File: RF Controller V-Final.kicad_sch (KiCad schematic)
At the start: 36 parts, among them J2 J_OLED, J3 BAT+, J4 BAT-, SW1 EG1218, U1 Teensy4.0, U3 NRF24L01, U5 AP2112K-3.3, U7 Pitch/Roll, U8 TPS542025DDCR, U9 Throttle/Yaw

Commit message: Modified regulator resistors
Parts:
- R6: value 13.3k -> 51.1k
- R7: value 100k -> 22k
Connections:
- net 9V_IN: now also R6.2; no longer R7.2
- net GND: now also R7.1; no longer R6.1
- new net: R6.1, R7.2, U8.5 (EN)
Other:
- moved on the sheet: R6, R7
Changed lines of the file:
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@@
 	)
 	(junction
-		(at 27.94 64.77)
+		(at 250.19 35.56)
 		(diameter 0)
 		(color 0 0 0 0)
 	)
 	(junction
-		(at 250.19 35.56)
+		(at 27.94 64.77)
 		(diameter 0)
 		(color 0 0 0 0)
@@
 	(wire
 		(pts
-			(xy 30.48 67.31) (xy 30.48 64.77)
-		)
-		(stroke
-			(width 0)
-			(type default)
-		)
-	)
-	(wire
-		(pts
 			(xy 213.36 82.55) (xy 212.09 82.55)
 		)
@@
 	(wire
 		(pts
-			(xy 27.94 72.39) (xy 30.48 72.39)
+			(xy 30.48 67.31) (xy 30.48 64.77)
 		)
 		(stroke
@@
 		)
 	)
-	(wire
-		(pts
-			(xy 27.94 63.5) (xy 27.94 64.77)
-		)
-		(stroke
-			(width 0)
-			(type default)
-		)
-	)
 	(polyline
 		(pts
@@
 		)
 	)
+	(wire
+		(pts
+			(xy 27.94 64.77) (xy 30.48 64.77)
+		)
+		(stroke
+			(width 0)
+			(type default)
+		)
+	)
 	(polyline
 		(pts
@@
 		)
 	)
+	(wire
+		(pts
+			(xy 27.94 63.5) (xy 27.94 64.77)
+		)
+		(stroke
+			(width 0)
+			(type default)
+		)
+	)
 	(polyline
 		(pts
@@
 		)
 	)
-	(wire
-		(pts
-			(xy 27.94 64.77) (xy 30.48 64.77)
-		)
-		(stroke
-			(width 0)
-			(type default)
-		)
-	)
 	(polyline
 		(pts
@@
 		)
 	)
+	(wire
+		(pts
+			(xy 27.94 72.39) (xy 30.48 72.39)
+		)
+		(stroke
+			(width 0)
+			(type default)
+		)
+	)
 	(polyline
 		(pts
@@
 	(symbol
 		(lib_id "Device:R")
-		(at 27.94 76.2 180)
+		(at 27.94 68.58 180)
 		(unit 1)
 		(body_style 1)
@@
 		(dnp no)
 		(property "Reference" "R6"
-			(at 24.638 77.47 0)
+			(at 24.638 69.85 0)
 			(show_name no)
 			(do_not_autoplace no)
@@
 			)
 		)
-		(property "Value" "13.3k"
-			(at 23.876 75.184 0)
+		(property "Value" "51.1k"
+			(at 23.876 67.564 0)
 			(show_name no)
 			(do_not_autoplace no)
@@
 		)
 		(property "Footprint" "Resistor_SMD:R_0805_2012Metric_Pad1.20x1.40mm_HandSolder"
-			(at 27.94 76.2 0)
+			(at 27.94 68.58 0)
 			(hide yes)
 			(show_name no)
@@
 		)
 		(property "Datasheet" ""
-			(at 27.94 76.2 0)
+			(at 27.94 68.58 0)
 			(hide yes)
 			(show_name no)
@@
 		)
 		(property "Description" "TPS542025 EN divider, VIN upper resistor"
-			(at 27.94 76.2 0)
+			(at 27.94 68.58 0)
 			(hide yes)
 			(show_name no)
@@
 	(symbol
 		(lib_id "Device:R")
-		(at 27.94 68.58 180)
+		(at 27.94 76.2 180)
 		(unit 1)
 		(body_style 1)
@@
 		(dnp no)
 		(property "Reference" "R7"
-			(at 26.416 69.85 0)
+			(at 26.416 77.47 0)
 			(show_name no)
 			(do_not_autoplace no)
@@
 			)
 		)
-		(property "Value" "100k"
-			(at 26.416 67.31 0)
+		(property "Value" "22k"
+			(at 26.416 74.93 0)
 			(show_name no)
 			(do_not_autoplace no)
@@
 		)
 		(property "Footprint" "Resistor_SMD:R_0805_2012Metric_Pad1.20x1.40mm_HandSolder"
-			(at 27.94 68.58 0)
+			(at 27.94 76.2 0)
 			(hide yes)
 			(show_name no)
@@
 		)
 		(property "Datasheet" ""
-			(at 27.94 68.58 0)
+			(at 27.94 76.2 0)
 			(hide yes)
 			(show_name no)
@@
 		)
 		(property "Description" "TPS542025 EN divider, ground lower resistor"
-			(at 27.94 68.58 0)
+			(at 27.94 76.2 0)
 			(hide yes)
 			(show_name no)
@@
 	)
 	(symbol
+		(lib_id "power:GND")
+		(at 27.94 80.01 0)
+		(unit 1)
+		(body_style 1)
+		(exclude_from_sim no)
+		(in_bom yes)
+		(on_board yes)
+		(in_pos_files yes)
+		(dnp no)
+		(fields_autoplaced yes)
+		(property "Reference" "#PWR05"
+			(at 27.94 86.36 0)
+			(hide yes)
+			(show_name no)
+			(do_not_autoplace no)
+			(effects
+				(font
+					(size 1.27 1.27)
+				)
+			)
+		)
+		(property "Value" "GND"
+			(at 27.94 85.09 0)
+			(show_name no)
+			(do_not_autoplace no)
+			(effects
+				(font
+					(size 1.27 1.27)
+				)
+			)
+		)
+		(property "Footprint" ""
+			(at 27.94 80.01 0)
+			(hide yes)
+			(show_name no)
+			(do_not_autoplace no)
+			(effects
+				(font
+					(size 1.27 1.27)
+				)
+			)
+		)
+		(property "Datasheet" ""
+			(at 27.94 80.01 0)
+			(hide yes)
+			(show_name no)
+			(do_not_autoplace no)
+			(effects
+				(font
+					(size 1.27 1.27)
+				)
+			)
+		)
+		(property "Description" "Power symbol creates a global label with name \"GND\" , ground"
+			(at 27.94 80.01 0)
+			(hide yes)
+			(show_name no)
+			(do_not_autoplace no)
+			(effects
+				(font
+					(size 1.27 1.27)
+				)
+			)
+		)
+		(pin "1"
+		)
+		(instances
+			(project "RF Controller V-Final"
+				(path "/20b51a64-697d-4081-9410-2d5c496e59fa"
+					(reference "#PWR05")
+					(unit 1)
+				)
+			)
+		)
+	)
+	(symbol
 		(lib_id "V2Components:TPS542025")
 		(at 40.64 69.85 0)
@@
 					(unit 1)
 				)
-			)
-		)
-	)
-	(symbol
-		(lib_id "power:GND")
-		(at 27.94 80.01 0)
-		(unit 1)
-		(body_style 1)
-		(exclude_from_sim no)
-		(in_bom yes)
-		(on_board yes)
-		(in_pos_files yes)
-		(dnp no)
-		(fields_autoplaced yes)
-		(property "Reference" "#PWR05"
-			(at 27.94 86.36 0)
-			(hide yes)
-			(show_name no)
-			(do_not_autoplace no)
-			(effects
-				(font
-					(size 1.27 1.27)
-				)
-			)
-		)
-		(property "Value" "GND"
-			(at 27.94 85.09 0)
-			(show_name no)
-			(do_not_autoplace no)
-			(effects
-				(font
-					(size 1.27 1.27)
-				)
-			)
-		)
-		(property "Footprint" ""
-			(at 27.94 80.01 0)
-			(hide yes)
-			(show_name no)
-			(do_not_autoplace no)
-			(effects
-				(font
-					(size 1.27 1.27)
-				)
-			)
-		)
-		(property "Datasheet" ""
-			(at 27.94 80.01 0)
-			(hide yes)
-			(show_name no)
-			(do_not_autoplace no)
-			(effects
-				(font
-					(size 1.27 1.27)
-				)
-			)
-		)
-		(property "Description" "Power symbol creates a global label with name \"GND\" , ground"
-			(at 27.94 80.01 0)
-			(hide yes)
-			(show_name no)
-			(do_not_autoplace no)
-			(effects
-				(font
-					(size 1.27 1.27)
-				)
-			)
-		)
-		(pin "1"
-		)
-		(instances
-			(project "RF Controller V-Final"
-				(path "/20b51a64-697d-4081-9410-2d5c496e59fa"
-					(reference "#PWR05")
-					(unit 1)
-				)

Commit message: Modified resistor for 5.5V EN startup
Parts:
- R6: value 51.1k -> 71.5k
- R7: value 22k -> 20k
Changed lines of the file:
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@@
 			)
 		)
-		(property "Value" "51.1k"
+		(property "Value" "71.5k"
 			(at 23.876 67.564 0)
 			(show_name no)
@@
 			)
 		)
-		(property "Value" "22k"
+		(property "Value" "20k"
 			(at 26.416 74.93 0)
 			(show_name no)

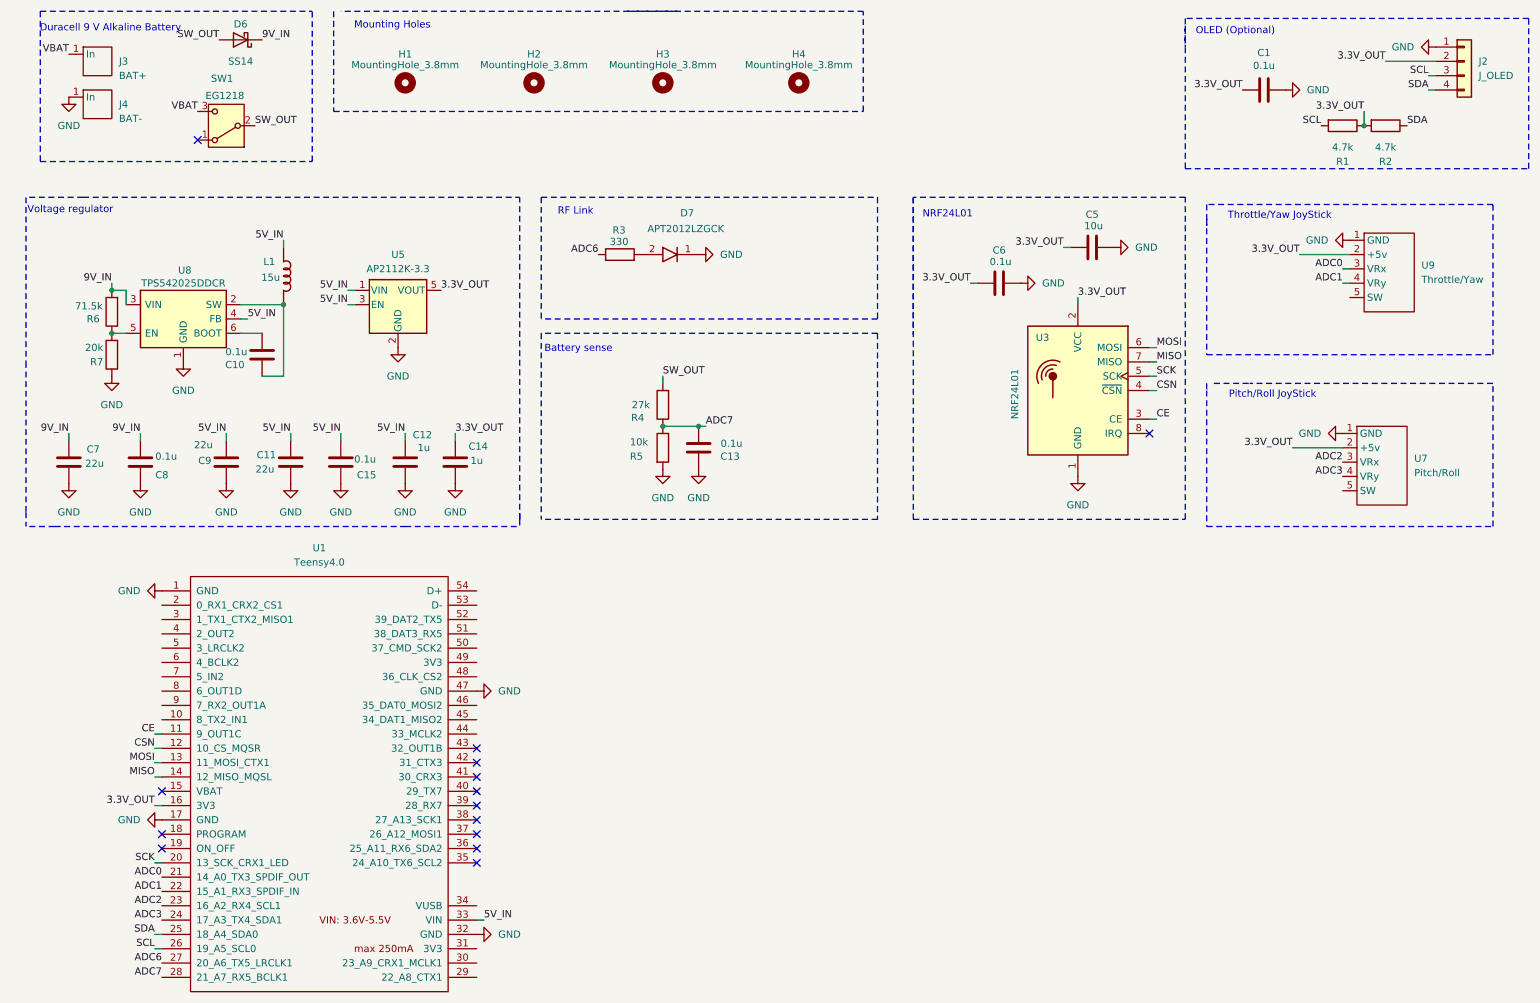
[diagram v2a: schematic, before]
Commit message: Added connections and changed cap values
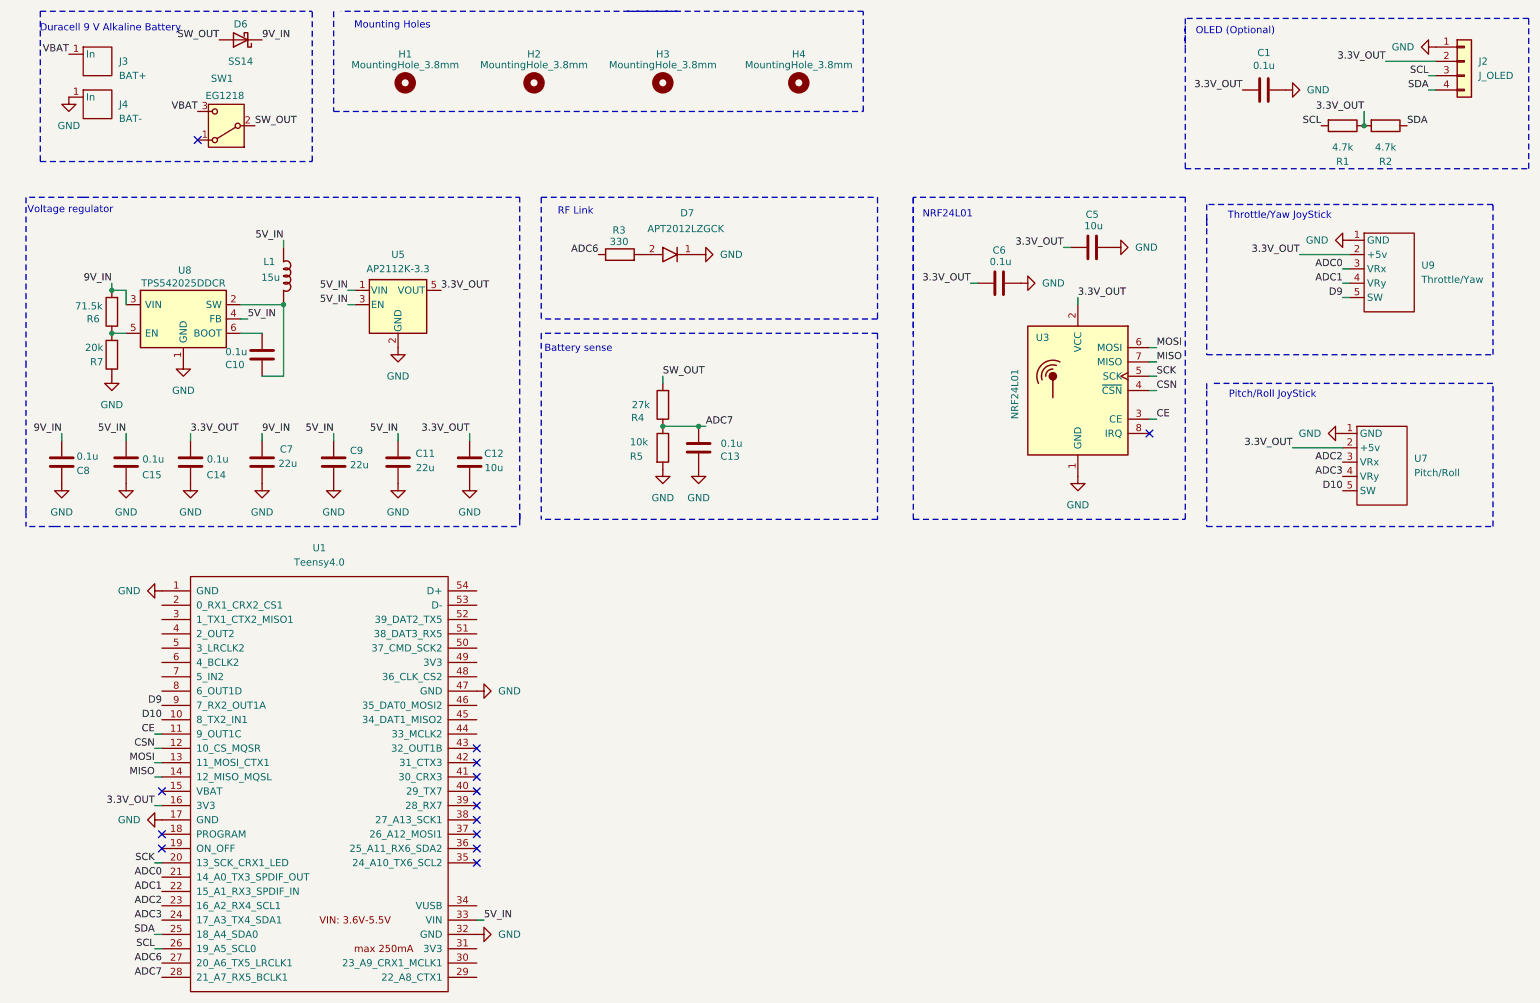
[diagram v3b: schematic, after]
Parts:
- C12: value 1u -> 10u
- C14: value 1u -> 0.1u
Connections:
- net 3.3V_OUT: now also C12.1
- net 5V_IN: no longer C12.1
- net D9: now reaches U9.5 (SW)
- net D9: now also U1.9 (7_RX2_OUT1A)
- net D10: now reaches U7.5 (SW)
- net D10: now also U1.10 (8_TX2_IN1)
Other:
- moved on the sheet: C11, C12, C14, C15, C7, C8, C9

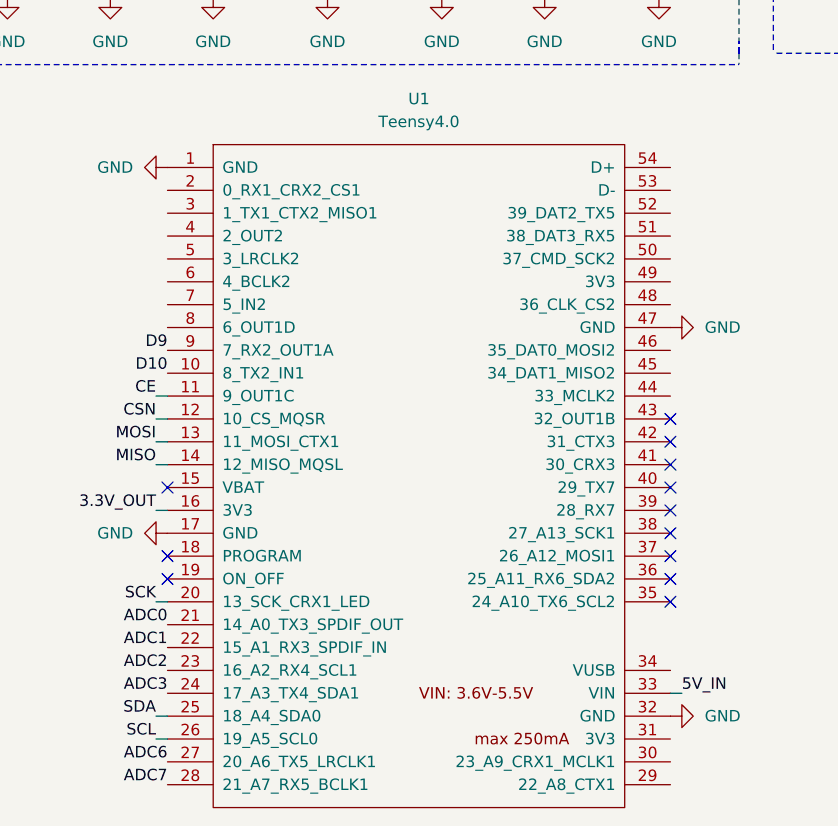
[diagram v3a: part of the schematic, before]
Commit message: Added components to PCB
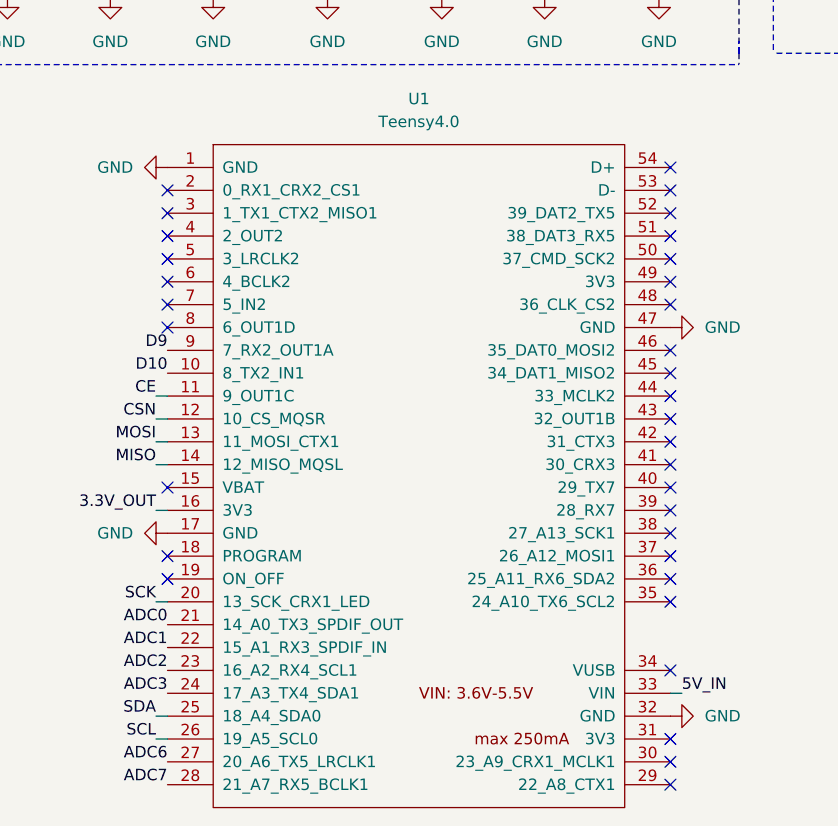
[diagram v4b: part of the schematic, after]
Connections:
- no-connect marks 14 -> 35
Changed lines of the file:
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@@
+	)
+	(no_connect
+		(at 92.71 118.11)
+	)
+	(no_connect
+		(at 92.71 143.51)
 	)
 	(no_connect
@@
 	)
 	(no_connect
+		(at 36.83 135.89)
+	)
+	(no_connect
 		(at 36.83 161.29)
 	)
@@
 	)
 	(no_connect
+		(at 36.83 123.19)
+	)
+	(no_connect
 		(at 92.71 156.21)
 	)
 	(no_connect
+		(at 92.71 181.61)
+	)
+	(no_connect
+		(at 92.71 120.65)
+	)
+	(no_connect
+		(at 92.71 133.35)
+	)
+	(no_connect
+		(at 92.71 140.97)
+	)
+	(no_connect
+		(at 92.71 138.43)
+	)
+	(no_connect
+		(at 36.83 133.35)
+	)
+	(no_connect
+		(at 36.83 130.81)
+	)
+	(no_connect
+		(at 92.71 128.27)
+	)
+	(no_connect
+		(at 36.83 125.73)
+	)
+	(no_connect
 		(at 43.18 38.1)
+	)
+	(no_connect
+		(at 92.71 125.73)
 	)
 	(no_connect
@@
 	)
 	(no_connect
+		(at 36.83 120.65)
+	)
+	(no_connect
+		(at 92.71 123.19)
+	)
+	(no_connect
+		(at 36.83 128.27)
+	)
+	(no_connect
 		(at 92.71 166.37)
+	)
+	(no_connect
+		(at 92.71 130.81)
+	)
+	(no_connect
+		(at 92.71 186.69)
 	)
 	(no_connect
@@
 		(at 92.71 148.59)
 	)
+	(no_connect
+		(at 92.71 184.15)
+	)
+	(no_connect
+		(at 92.71 173.99)
+	)
 	(wire
